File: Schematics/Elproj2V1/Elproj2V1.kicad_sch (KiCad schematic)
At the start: 22 parts, among them J1 Conn_01x04_Pin, J2 Conn_01x04_Pin, J3 Conn_01x04_Pin, J4 Conn_01x04_Pin, J5 Conn_01x04_Pin, Q1 PMOS, Q2 NMOS, SW2 Manual, U1 MOUDLE-SEEEDUINO-XIAO-ESP32C3

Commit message: Update Elproj2V1.kicad_sch
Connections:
- net GND: now also C1.2, J2.2 (Pin_2), J3.2 (Pin_2), J4.2 (Pin_2), J5.2 (Pin_2)
- net Cap_BOOSTED_PWR: now reaches J3.1 (Pin_1)
- net Cap_BOOSTED_PWR: now also J2.1 (Pin_1), J4.1 (Pin_1), J5.1 (Pin_1)
- net Coil_Sense_4: now reaches U1.10 (PA5_A9_D9_MISO)
- net Coil_Sense_4: now also J5.3 (Pin_3)
- net Coil_Act_4: now reaches U1.11 (PA6_A10_D10_MOSI)
- net Coil_Act_4: now also J5.4 (Pin_4)
- net Coil_Sense_1: now reaches U1.2 (PA4_A1_D1)
- net Coil_Sense_1: now also J2.3 (Pin_3)
- net Coil_Act_1: now reaches U1.3 (PA10_A2_D2)
- net Coil_Act_1: now also J2.4 (Pin_4)
- net Coil_Sense_2: now reaches U1.4 (PA11_A3_D3)
- net Coil_Sense_2: now also J3.3 (Pin_3)
- net Coil_Act_2: now reaches U1.5 (PA8_A4_D4_SDA)
- net Coil_Act_2: now also J3.4 (Pin_4)
- net Coil_Sense_3: now reaches U1.6 (PA9_A5_D5_SCL)
- net Coil_Sense_3: now also J4.3 (Pin_3)
- net Coil_Act_3: now reaches U1.7 (PB08_A6_D6_TX)
- net Coil_Act_3: now also J4.4 (Pin_4)
- new net Cap_PWR: C1.1
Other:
- moved on the sheet: J2, U1

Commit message: starting buck stuff
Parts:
- added C2, C3: 22uF, symbol Device:C_Small
- added C4: 470uF, symbol Device:C_Polarized_US
- added C5: 4.7uF, symbol Device:C_Small
- added C6: 10uF, symbol Device:C_Small
- added C7: 0.1uF, symbol Device:C_Small
- added L1: 6.8uH, symbol Device:L_Iron
- added R6: 1M, symbol Device:R_Small
- added R8: 100k, symbol Device:R_Small
- added U2: TPS61088RHLR, TPS61088RHLR:IC_TPS61088RHLR, symbol TPS61088RHLR:TPS61088RHLR
- added U3: TLV61220DBVR, TLV61220DBVR:SOT95P280X145-6N, symbol TLV61220DBVR:TLV61220DBVR
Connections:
- net GND: no longer C1.2, J2.2 (Pin_2), J3.2 (Pin_2), J4.2 (Pin_2), J5.2 (Pin_2)
- new net: C5.2, L1.1, U3.1 (SW)
- new net: C2.1, C3.1, C4.1, L1.2, U3.3 (EN), U3.6 (VBAT)
- new net: U2.21 (PGND), U2.22 (PGND), U2.23 (PGND), U2.24 (PGND), U2.25 (PGND), U2.26 (PGND), U2.27 (PGND), U2.28 (PGND), U2.29 (PGND)
- new net: C6.1, C7.1, R6.1, U3.5 (VOUT)
- new net: C6.2, C7.2
- new net: R6.2, R8.1, U3.4 (FB)
- new net GNDA: C5.1, R8.2, U3.2 (GND)
- new net GNDPWR: C2.2, C3.2, C4.2, J2.2 (Pin_2), J3.2 (Pin_2), J4.2 (Pin_2), J5.2 (Pin_2)
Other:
- moved on the sheet: C1, J2, J3, J4, J5, U1

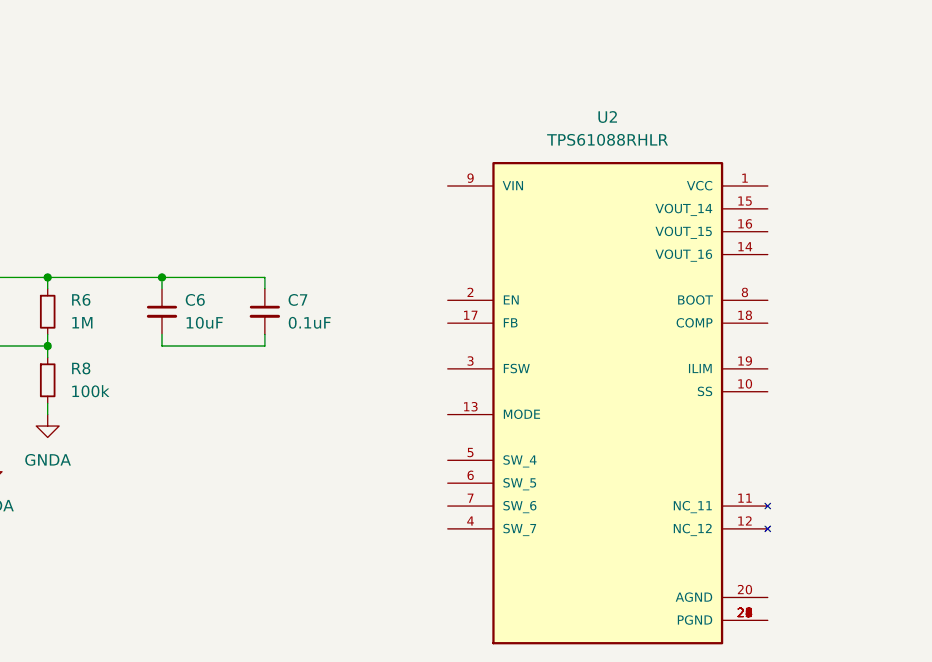
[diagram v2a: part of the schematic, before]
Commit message: Fixed TPS symbol
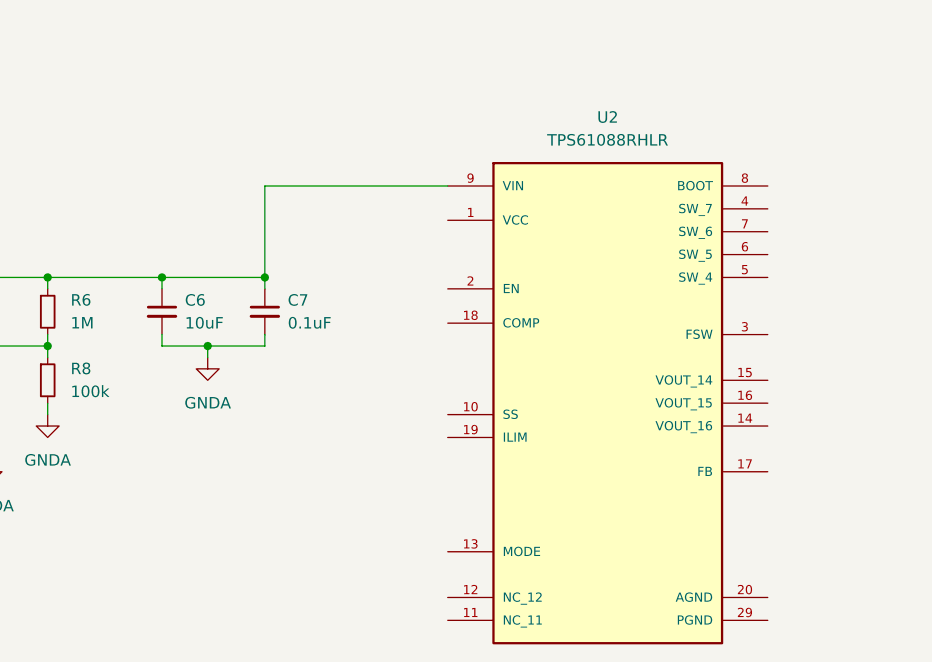
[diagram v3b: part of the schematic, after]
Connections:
- net GNDA: now also C6.2, C7.2
- net at U2.9 (VIN): now also C6.1, C7.1, R6.1, U3.5 (VOUT)
- now unconnected: U2.29 (PGND)
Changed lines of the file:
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@@
   (junction (at 74.93 45.72) (diameter 0) (color 0 0 0 0)
   )
+  (junction (at 152.4 177.8) (diameter 0) (color 0 0 0 0)
+  )
   (junction (at 218.44 36.83) (diameter 0) (color 0 0 0 0)
   )
@@
   (junction (at 214.63 39.37) (diameter 0) (color 0 0 0 0)
   )
+  (junction (at 146.05 185.42) (diameter 0) (color 0 0 0 0)
+  )
   (junction (at 87.63 182.88) (diameter 0) (color 0 0 0 0)
   )
@@
     (stroke (width 0) (type default))
   )
+  (wire (pts (xy 172.72 167.64) (xy 152.4 167.64))
+    (stroke (width 0) (type default))
+  )
   (wire (pts (xy 26.67 29.21) (xy 29.845 29.21))
     (stroke (width 0) (type default))
@@
     (stroke (width 0) (type default))
   )
+  (wire (pts (xy 152.4 167.64) (xy 152.4 177.8))
+    (stroke (width 0) (type default))
+  )
   (wire (pts (xy 26.67 26.67) (xy 29.845 26.67))
     (stroke (width 0) (type default))
@@
     (stroke (width 0) (type default))
   )
+  (wire (pts (xy 146.05 185.42) (xy 152.4 185.42))
+    (stroke (width 0) (type default))
+  )
   (wire (pts (xy 73.025 80.645) (xy 75.565 80.645))
     (stroke (width 0) (type default))
@@
     (stroke (width 0) (type default))
   )
-  (wire (pts (xy 140.97 185.42) (xy 152.4 185.42))
+  (wire (pts (xy 140.97 185.42) (xy 146.05 185.42))
     (stroke (width 0) (type default))
   )
@@
   )
   (wire (pts (xy 127 26.67) (xy 129.54 26.67))
+    (stroke (width 0) (type default))
+  )
+  (wire (pts (xy 146.05 185.42) (xy 146.05 186.69))
     (stroke (width 0) (type default))
   )
@@
       (effects (font (size 1.27 1.27)))
     )
-    (property "Footprint" "TPS61088RHLR:IC_TPS61088RHLR" (at 190.5 190.5 0)
+    (property "Footprint" "TPS61088RHLR:IC_TPS61088RHLR" (at 190.5 154.94 0)
       (effects (font (size 1.27 1.27)) (justify bottom) hide)
     )
@@
       (effects (font (size 1.27 1.27)) hide)
     )
-    (property "MF" "Texas Instruments" (at 190.5 190.5 0)
-      (effects (font (size 1.27 1.27)) (justify bottom) hide)
-    )
-    (property "MAXIMUM_PACKAGE_HEIGHT" "1.00mm" (at 190.5 190.5 0)
-      (effects (font (size 1.27 1.27)) (justify bottom) hide)
-    )
-    (property "Package" "VQFN-20 Texas Instruments" (at 190.5 190.5 0)
-      (effects (font (size 1.27 1.27)) (justify bottom) hide)
-    )
-    (property "Price" "None" (at 190.5 190.5 0)
-      (effects (font (size 1.27 1.27)) (justify bottom) hide)
-    )
-    (property "Check_prices" "https://www.snapeda.com/parts/TPS61088RHLR/Texas+Instruments/view-part/?ref=eda" (at 190.5 190.5 0)
-      (effects (font (size 1.27 1.27)) (justify bottom) hide)
-    )
-    (property "STANDARD" "Manufacturer Recommendations" (at 190.5 190.5 0)
-      (effects (font (size 1.27 1.27)) (justify bottom) hide)
-    )
-    (property "PARTREV" "4219071/A 05/2017" (at 190.5 190.5 0)
-      (effects (font (size 1.27 1.27)) (justify bottom) hide)
-    )
-    (property "SnapEDA_Link" "https://www.snapeda.com/parts/TPS61088RHLR/Texas+Instruments/view-part/?ref=snap" (at 190.5 190.5 0)
-      (effects (font (size 1.27 1.27)) (justify bottom) hide)
-    )
-    (property "MP" "TPS61088RHLR" (at 190.5 190.5 0)
-      (effects (font (size 1.27 1.27)) (justify bottom) hide)
-    )
-    (property "Purchase-URL" "https://www.snapeda.com/api/url_track_click_mouser/?unipart_id=229898&manufacturer=Texas Instruments&part_name=TPS61088RHLR&search_term=tps61088" (at 190.5 190.5 0)
-      (effects (font (size 1.27 1.27)) (justify bottom) hide)
-    )
-    (property "Description" "\n10-A Fully-Integrated Synchronous Boost Converter\n" (at 190.5 190.5 0)
-      (effects (font (size 1.27 1.27)) (justify bottom) hide)
-    )
-    (property "Availability" "In Stock" (at 190.5 190.5 0)
-      (effects (font (size 1.27 1.27)) (justify bottom) hide)
-    )
-    (property "MANUFACTURER" "Texas Instruments" (at 190.5 190.5 0)
+    (property "MF" "Texas Instruments" (at 189.23 156.21 0)
+      (effects (font (size 1.27 1.27)) (justify bottom) hide)
+    )
+    (property "MAXIMUM_PACKAGE_HEIGHT" "1.00mm" (at 190.5 157.48 0)
+      (effects (font (size 1.27 1.27)) (justify bottom) hide)
+    )
+    (property "Package" "VQFN-20 Texas Instruments" (at 191.77 157.48 0)
+      (effects (font (size 1.27 1.27)) (justify bottom) hide)
+    )
+    (property "Price" "None" (at 189.23 156.21 0)
+      (effects (font (size 1.27 1.27)) (justify bottom) hide)
+    )
+    (property "Check_prices" "https://www.snapeda.com/parts/TPS61088RHLR/Texas+Instruments/view-part/?ref=eda" (at 186.69 157.48 0)
+      (effects (font (size 1.27 1.27)) (justify bottom) hide)
+    )
+    (property "STANDARD" "Manufacturer Recommendations" (at 191.77 156.21 0)
+      (effects (font (size 1.27 1.27)) (justify bottom) hide)
+    )
+    (property "PARTREV" "4219071/A 05/2017" (at 190.5 157.48 0)
+      (effects (font (size 1.27 1.27)) (justify bottom) hide)
+    )
+    (property "SnapEDA_Link" "https://www.snapeda.com/parts/TPS61088RHLR/Texas+Instruments/view-part/?ref=snap" (at 189.23 156.21 0)
+      (effects (font (size 1.27 1.27)) (justify bottom) hide)
+    )
+    (property "MP" "TPS61088RHLR" (at 190.5 157.48 0)
+      (effects (font (size 1.27 1.27)) (justify bottom) hide)
+    )
+    (property "Purchase-URL" "https://www.snapeda.com/api/url_track_click_mouser/?unipart_id=229898&manufacturer=Texas Instruments&part_name=TPS61088RHLR&search_term=tps61088" (at 189.23 156.21 0)
+      (effects (font (size 1.27 1.27)) (justify bottom) hide)
+    )
+    (property "Description" "\n10-A Fully-Integrated Synchronous Boost Converter\n" (at 190.5 154.94 0)
+      (effects (font (size 1.27 1.27)) (justify bottom) hide)
+    )
+    (property "Availability" "In Stock" (at 187.96 154.94 0)
+      (effects (font (size 1.27 1.27)) (justify bottom) hide)
+    )
+    (property "MANUFACTURER" "Texas Instruments" (at 189.23 157.48 0)
       (effects (font (size 1.27 1.27)) (justify bottom) hide)
     )
@@
     (pin "2")
     (pin "20")
-    (pin "21")
-    (pin "22")
-    (pin "23")
-    (pin "24")
-    (pin "25")
-    (pin "26")
-    (pin "27")
-    (pin "28")
     (pin "29")
     (pin "3")
@@
         )
       )
+    )
+  )
+  (symbol (lib_id "power:GNDA") (at 146.05 186.69 0) (unit 1)
+    (in_bom yes) (on_board yes) (dnp no) (fields_autoplaced)
+    (property "Reference" "#PWR016" (at 146.05 193.04 0)
+      (effects (font (size 1.27 1.27)) hide)
+    )
+    (property "Value" "GNDA" (at 146.05 191.77 0)
+      (effects (font (size 1.27 1.27)))
+    )
+    (property "Footprint" "" (at 146.05 186.69 0)
+      (effects (font (size 1.27 1.27)) hide)
+    )
+    (property "Datasheet" "" (at 146.05 186.69 0)
+      (effects (font (size 1.27 1.27)) hide)
+    )
+    (pin "1")
+    (instances
+      (project "Elproj2V1"
+        (path "/f0d7dc79-2865-4dd1-b2c5-de9bb2b6a418"
+          (reference "#PWR016") (unit 1)
+        )
+      )

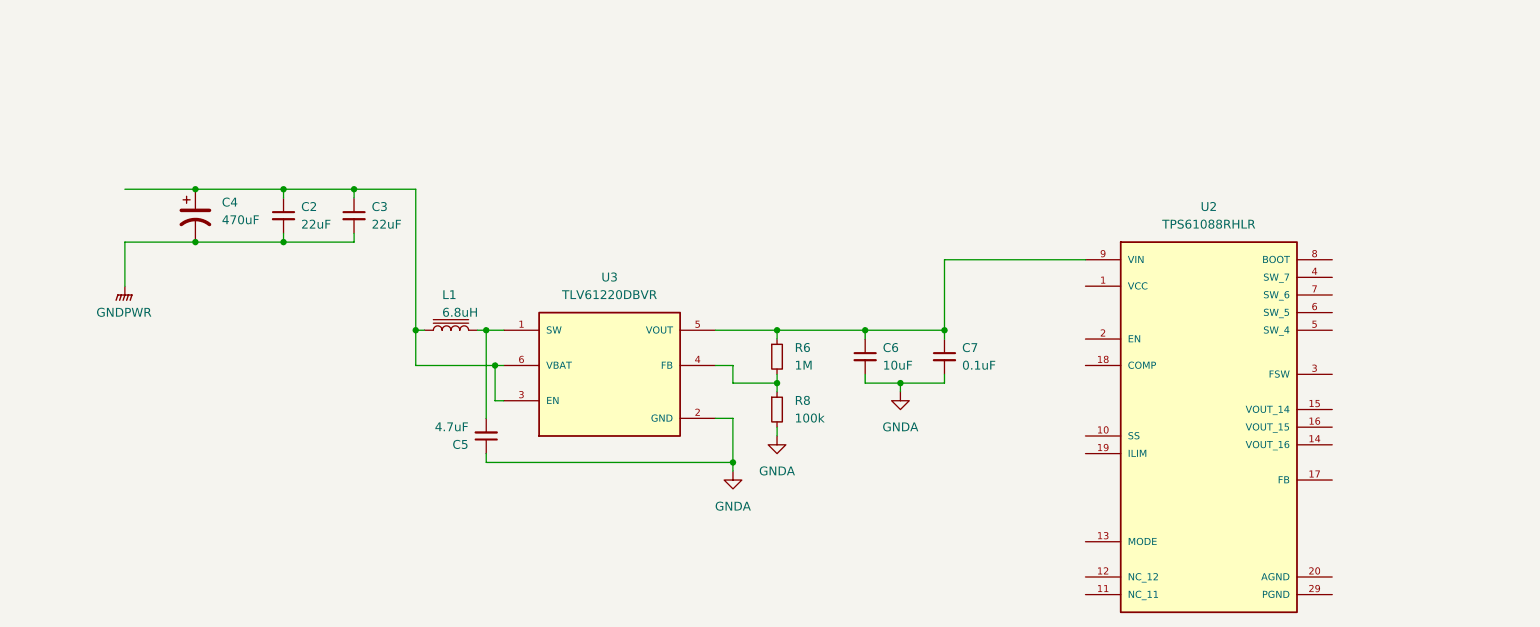
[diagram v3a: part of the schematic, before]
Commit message: added left side of buck
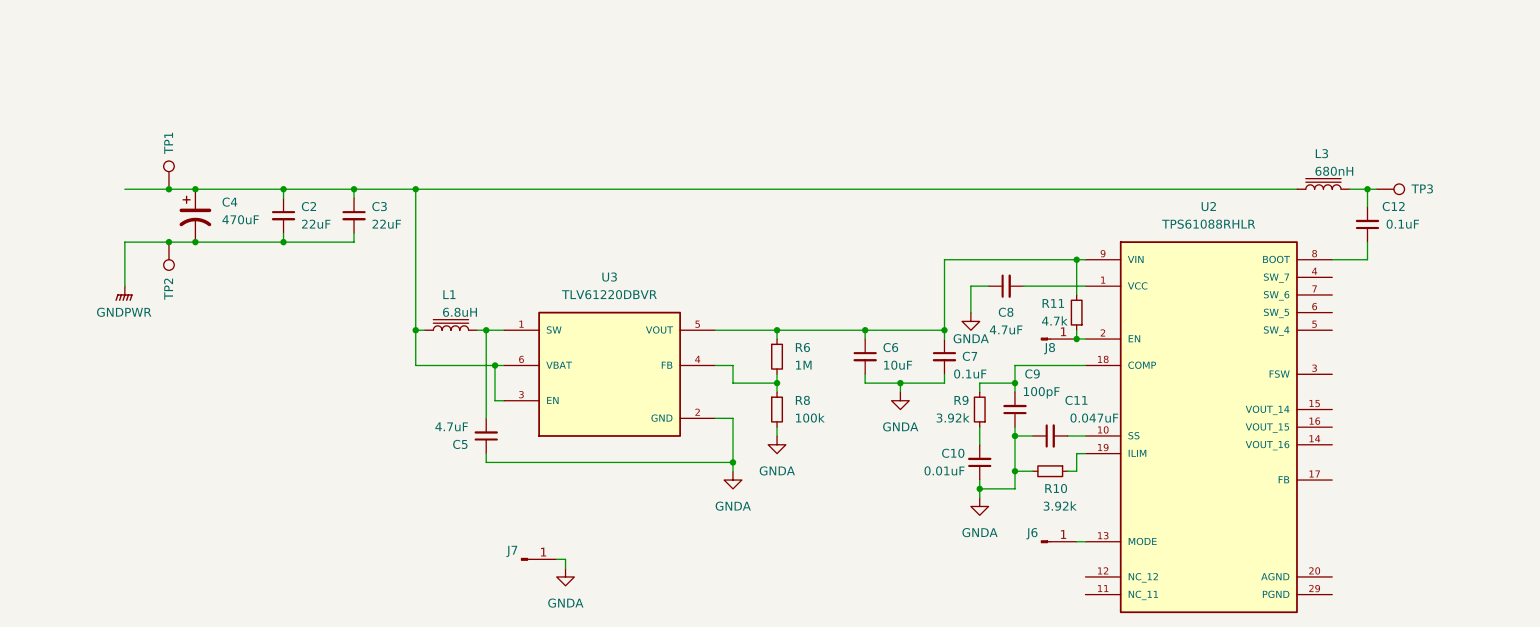
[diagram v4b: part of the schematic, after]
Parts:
- added C10: 0.01uF, symbol Device:C_Small
- added C11: 0.047uF, symbol Device:C_Small
- added C12: 0.1uF, symbol Device:C_Small
- added C8: 4.7uF, symbol Device:C_Small
- added C9: 100pF, symbol Device:C_Small
- added J6, J7: Conn_01x01_Pin, symbol Connector:Conn_01x01_Pin
- added J8: EN, symbol Connector:Conn_01x01_Pin
- added L3: 680nH, symbol Device:L_Iron
- added R10, R9: 3.92k, symbol Device:R_Small
- added R11: 4.7k, symbol Device:R_Small
- added TP1, TP2, TP3: TP3, symbol Connector:TestPoint
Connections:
- net GNDA: now also C10.1, C11.1, C8.1, C9.1, J7.1 (Pin_1), R10.2
- net GNDPWR: now also TP2.1
- net at C2.1, C3.1, C4.1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: now also L3.2, TP1.1
- net at U2.1 (VCC): now also C8.2
- net at U2.10 (SS): now also C11.2
- net at U2.13 (MODE): now also J6.1 (Pin_1)
- net at U2.18 (COMP): now also C9.2, R9.2
- net at U2.19 (ILIM): now also R10.1
- net at U2.2 (EN): now also J8.1 (Pin_1), R11.1
- net at U2.8 (BOOT): now also C12.1
- net at C6.1, C7.1, R6.1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: now also R11.2
- new net: C10.2, R9.1
- new net: C12.2, L3.1, TP3.1

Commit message: Update Elproj2V1.kicad_sch
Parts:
- added D4: 6V, symbol Device:D_Zener
- added D5: RED LED, symbol Device:LED
- added R12: 4.7k, symbol Device:R_Small
- added R13, R14, R15: 10, symbol Device:R_Small
- added SW1: SW_DPDT_x2, symbol Switch:SW_DPDT_x2
- C1: value Super Konding -> 2.5F; Note (none) -> Super Kondingen
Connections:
- net Cap_PWR: now also SW1.1 (A); no longer C1.1
- net GNDPWR: now also C1.2, D5.1 (K)
- new net: C1.1, SW1.2 (B)
- new net: D4.2 (A), R13.1, R14.1, R15.1, SW1.3 (C)
- new net: R13.2, R14.2, R15.2
- new net: D4.1 (K), R12.1
- new net: D5.2 (A), R12.2

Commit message: Fixade in Nicklas Grejer
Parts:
- added C13: 1µF, symbol Device:C
- added C14, C15, C17: 22µF, symbol Device:C
- added C16: 1000pF, symbol Device:C
- added C18: Not in use, symbol Device:C
- added R16: 301k, symbol Device:R_Small
- added R17: 56.2k, symbol Device:R_Small
- added R18, R19: R_Small, symbol Device:R_Small
- added R20: 49.9, symbol Device:R_Small
- added R21: 97.6, symbol Device:R_Small
- added TP4, TP5: ~, symbol Connector:TestPoint
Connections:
- net Cap_BOOSTED_PWR: now also U2.15 (VOUT_14), C13.1, C14.1, C15.1, C17.1, R20.1
- net GNDA: now also U2.11 (NC_11), U2.12 (NC_12), U2.20 (AGND), U2.29 (PGND), R17.2
- net GNDPWR: now also C13.2, C14.2, C15.2, C16.2, C17.2, TP5.1
- net at U2.17 (FB): now also C18.2, R17.1, R21.2
- net at U2.3 (FSW): now also R16.2
- net at U2.4 (SW_7): now also U2.5 (SW_4), U2.6 (SW_5), U2.7 (SW_6), R16.1, R18.1, R19.1
- new net: C16.1, R18.2, R19.2
- new net: C18.1, R20.2, R21.1, TP4.1
